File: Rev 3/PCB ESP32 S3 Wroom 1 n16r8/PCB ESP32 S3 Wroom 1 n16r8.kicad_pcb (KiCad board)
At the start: 2 copper layers, 80.5 x 89.5 mm, 37 parts, among them J1 AudioJack3_SwitchT, M1 Haptic Feedback, Q1 BS170, SW1 Home, SW2 Back, SW3 Play/Pause, SW4 Power, SW5 Menu, SW6 Hold, SW7 BOOT_MODE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

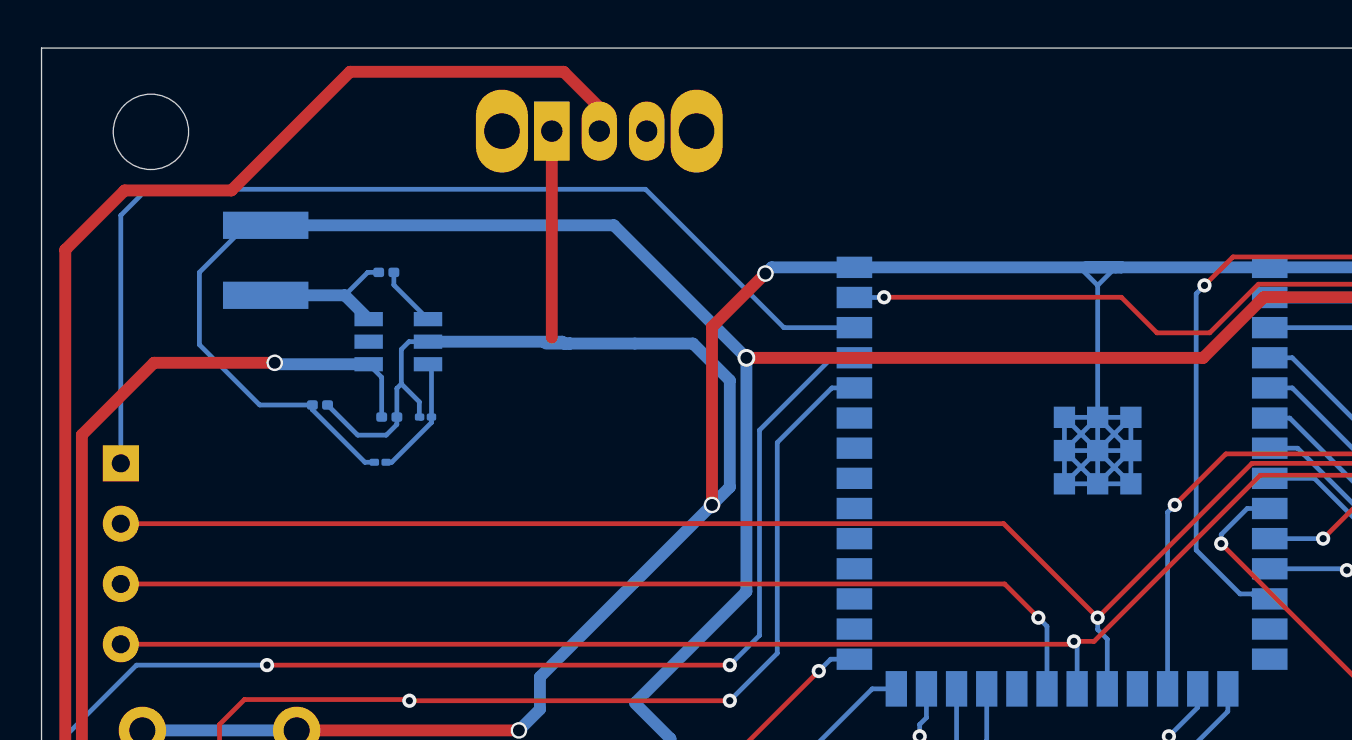
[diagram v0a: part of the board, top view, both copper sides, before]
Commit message: updated power regulator circuit
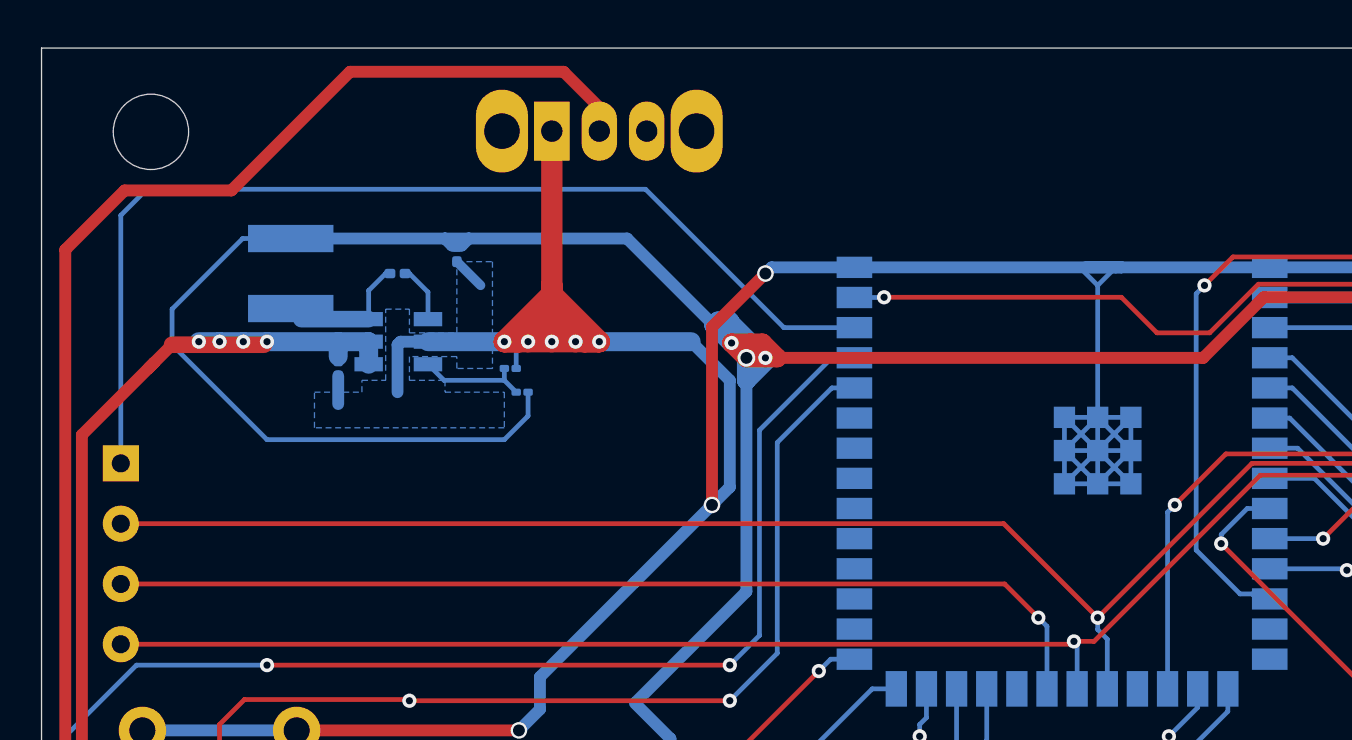
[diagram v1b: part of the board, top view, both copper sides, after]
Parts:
- moved C3 8.59 mm to (76.0, 51.7), turned to 90 degrees
- moved R14 6.67 mm to (78.8, 57.5), turned to 0 degrees
- moved R15 4.12 mm to (78.2, 56.5), turned to 180 degrees
- moved C2 2.97 mm to (71.0, 56.5), turned to 90 degrees
- moved L1 1.19 mm to (69.0, 52.5)
- moved C1 0.48 mm to (73.5, 52.5)
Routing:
- net /VDD: track 359.7 -> 377.0 mm, vias 4 -> 6
- net GND: track 312.9 -> 328.1 mm, vias 3 -> 8
- net /5V: track 99.2 -> 101.8 mm, vias 1 -> 4
- net Net-(U1-SW): track 6.58 -> 5.87 mm
- added copper zone on B.Cu, net GND

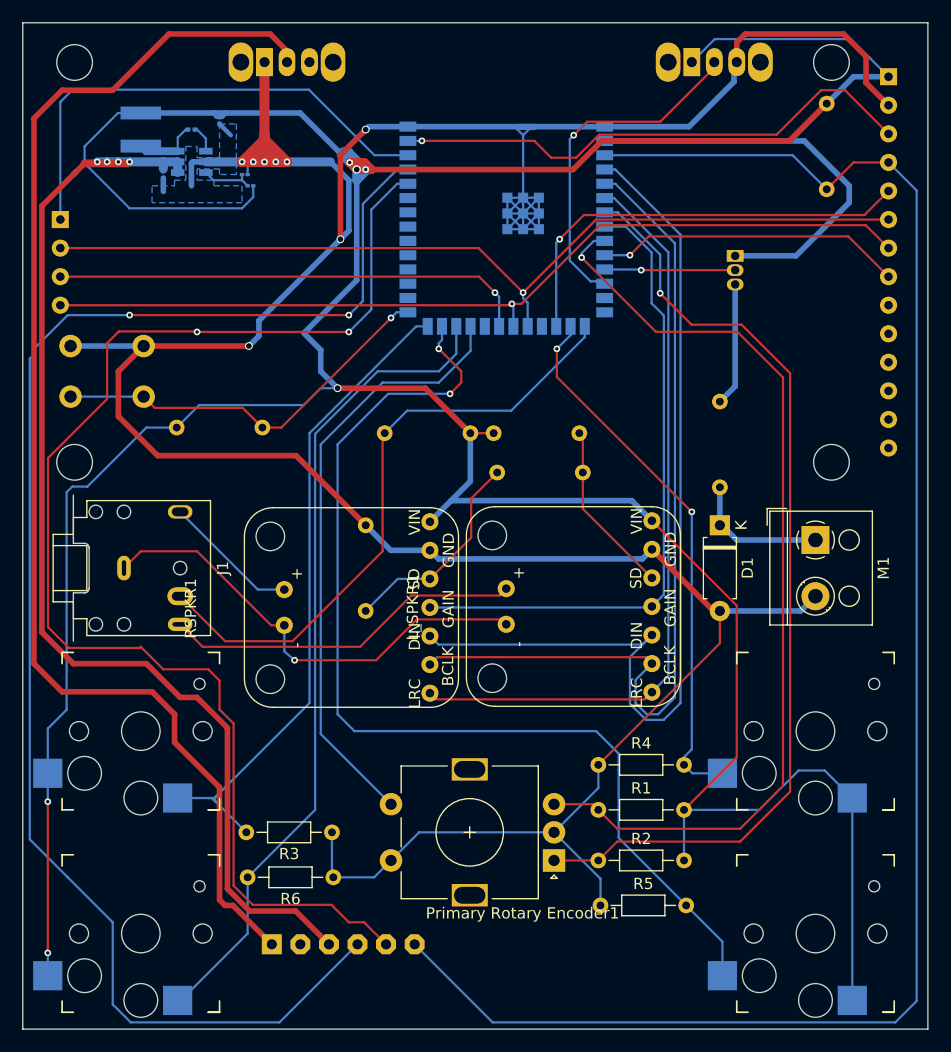
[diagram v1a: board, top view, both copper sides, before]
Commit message: added esp to BOM
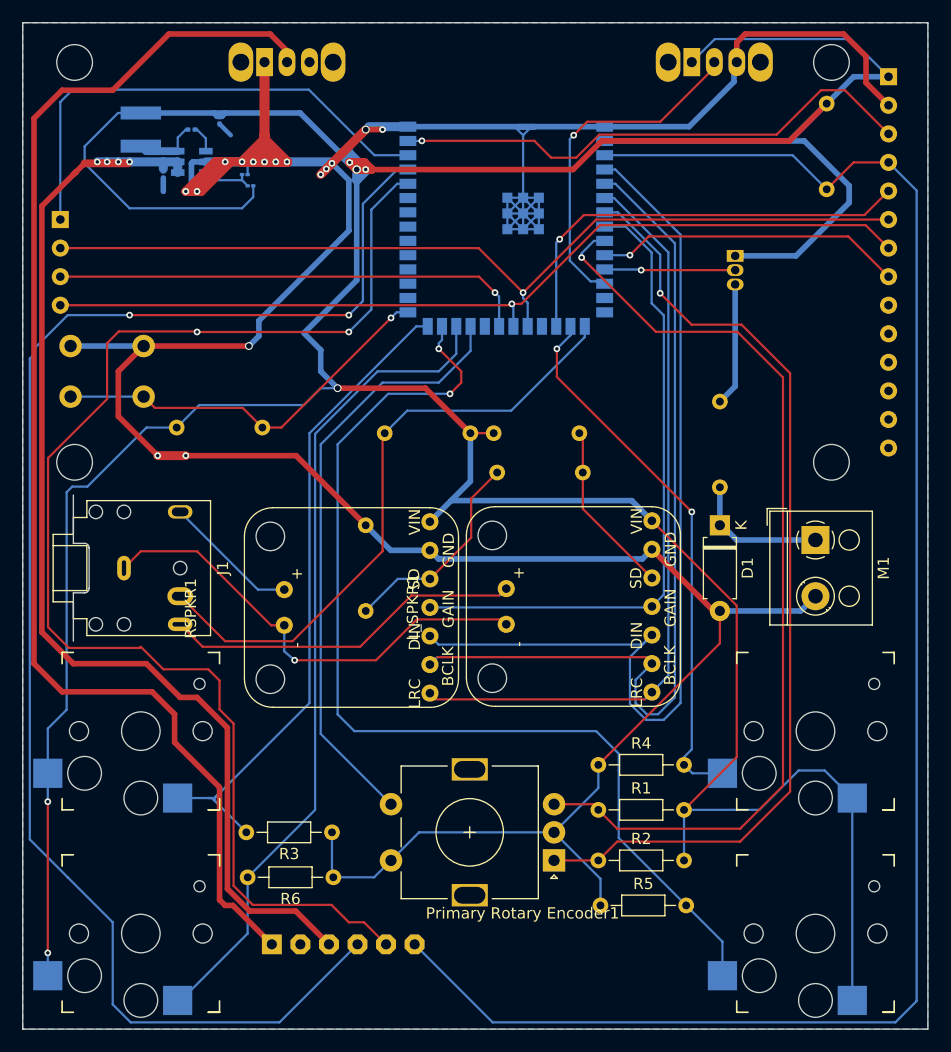
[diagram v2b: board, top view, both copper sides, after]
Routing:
- net GND: track 328.1 -> 340.5 mm, vias 8 -> 16
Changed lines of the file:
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@@
 	)
 	(segment
-		(start 86.75 54.75)
-		(end 89 52.5)
-		(width 0.5)
+		(start 85 56.5)
+		(end 85.5 56)
+		(width 0.8)
 		(layer "F.Cu")
 		(net 7)
@@
 	)
 	(segment
-		(start 67 78)
-		(end 67 74)
-		(width 0.5)
+		(start 73 58)
+		(end 73.5 58)
+		(width 0.8)
 		(layer "F.Cu")
 		(net 7)
@@
 	)
 	(segment
+		(start 67 74)
+		(end 67 78)
+		(width 0.5)
+		(layer "F.Cu")
+		(net 7)
+	)
+	(segment
 		(start 80 54)
 		(end 81.372 55.372)
@@
 	)
 	(segment
+		(start 73 81.5)
+		(end 70.5 81.5)
+		(width 0.8)
+		(layer "F.Cu")
+		(net 7)
+	)
+	(segment
 		(start 119.9315 95.31)
 		(end 120.5 95.31)
@@
 	)
 	(segment
-		(start 86.75 62.25)
-		(end 86.75 54.75)
-		(width 0.5)
-		(layer "F.Cu")
-		(net 7)
-	)
-	(segment
 		(start 80 53.372)
 		(end 82 55.372)
@@
 	)
 	(segment
+		(start 73 58)
+		(end 75.628 55.372)
+		(width 0.8)
+		(layer "F.Cu")
+		(net 7)
+	)
+	(segment
 		(start 89 87.69)
 		(end 82.81 81.5)
@@
 	)
 	(segment
+		(start 69.25 71.75)
+		(end 67 74)
+		(width 0.5)
+		(layer "F.Cu")
+		(net 7)
+	)
+	(segment
+		(start 76.128 55.372)
+		(end 77 55.372)
+		(width 0.8)
+		(layer "F.Cu")
+		(net 7)
+	)
+	(segment
 		(start 81.372 55.372)
 		(end 82 55.372)
@@
 	)
 	(segment
+		(start 85.5 56)
+		(end 86 55.5)
+		(width 0.8)
+		(layer "F.Cu")
+		(net 7)
+	)
+	(segment
 		(start 80 54)
 		(end 78.628 55.372)
@@
 	)
 	(segment
-		(start 67 74)
-		(end 69.25 71.75)
+		(start 133.5 48.34)
+		(end 133.5 46)
 		(width 0.5)
 		(layer "F.Cu")
@@
 	)
 	(segment
-		(start 133.5 48.34)
-		(end 133.5 46)
-		(width 0.5)
+		(start 73.5 58)
+		(end 76.128 55.372)
+		(width 0.8)
 		(layer "F.Cu")
 		(net 7)
@@
 	)
 	(segment
+		(start 67 78)
+		(end 70.5 81.5)
+		(width 0.5)
+		(layer "F.Cu")
+		(net 7)
+	)
+	(segment
+		(start 86 55.5)
+		(end 89 52.5)
+		(width 0.8)
+		(layer "F.Cu")
+		(net 7)
+	)
+	(segment
+		(start 77 55.372)
+		(end 79 55.372)
+		(width 0.8)
+		(layer "F.Cu")
+		(net 7)
+	)
+	(segment
 		(start 80 53)
 		(end 80 54)
@@
 	)
 	(segment
-		(start 70.5 81.5)
-		(end 67 78)
-		(width 0.5)
+		(start 74 58)
+		(end 74.372 58)
+		(width 0.8)
 		(layer "F.Cu")
 		(net 7)
@@
 	)
 	(segment
+		(start 74.372 58)
+		(end 77 55.372)
+		(width 0.8)
+		(layer "F.Cu")
+		(net 7)
+	)
+	(segment
 		(start 80 54.372)
 		(end 79 55.372)
@@
 	)
 	(segment
+		(start 89 52.5)
+		(end 90.5 52.5)
+		(width 0.5)
+		(layer "F.Cu")
+		(net 7)
+	)
+	(segment
 		(start 135.5 50.34)
 		(end 133.5 48.34)
@@
 	)
 	(segment
+		(start 73.5 58)
+		(end 74 58)
+		(width 0.8)
+		(layer "F.Cu")
+		(net 7)
+	)
+	(segment
 		(start 120.5 95.31)
 		(end 120.5 98.19)
@@
 	)
 	(segment
+		(start 75.628 55.372)
+		(end 76.128 55.372)
+		(width 0.8)
+		(layer "F.Cu")
+		(net 7)
+	)
+	(segment
 		(start 82.81 81.5)
-		(end 70.5 81.5)
+		(end 73 81.5)
 		(width 0.5)
 		(layer "F.Cu")
@@
 	)
 	(via
+		(at 86 55.5)
+		(size 0.6)
+		(drill 0.3)
+		(layers "F.Cu" "B.Cu")
+		(net 7)
+	)
+	(via
 		(at 89 52.5)
 		(size 0.7)
@@
 	)
 	(via
+		(at 73 81.5)
+		(size 0.6)
+		(drill 0.3)
+		(layers "F.Cu" "B.Cu")
+		(net 7)
+	)
+	(via
+		(at 76.5 55.372)
+		(size 0.6)
+		(drill 0.3)
+		(layers "F.Cu" "B.Cu")
+		(net 7)
+	)
+	(via
 		(at 78 55.372)
 		(size 0.6)
@@
 	)
 	(via
+		(at 85.5 56)
+		(size 0.6)
+		(drill 0.3)
+		(layers "F.Cu" "B.Cu")
+		(net 7)
+	)
+	(via
 		(at 82 55.372)
 		(size 0.6)
@@
 	)
 	(via
-		(at 86.75 62.25)
+		(at 78.613 71.75)
 		(size 0.7)
 		(drill 0.5)
@@
 	)
 	(via
-		(at 78.613 71.75)
-		(size 0.7)
-		(drill 0.5)
+		(at 85 56.5)
+		(size 0.6)
+		(drill 0.3)
+		(layers "F.Cu" "B.Cu")
+		(net 7)
+	)
+	(via
+		(at 74 58)
+		(size 0.6)
+		(drill 0.3)
+		(layers "F.Cu" "B.Cu")
+		(free yes)
+		(net 7)
+	)
+	(via
+		(at 70.5 81.5)
+		(size 0.6)
+		(drill 0.3)
+		(layers "F.Cu" "B.Cu")
+		(net 7)
+	)
+	(via
+		(at 73 58)
+		(size 0.6)
+		(drill 0.3)
+		(layers "F.Cu" "B.Cu")
+		(free yes)
+		(net 7)
+	)
+	(via
+		(at 90.5 52.5)
+		(size 0.6)
+		(drill 0.3)
 		(layers "F.Cu" "B.Cu")
 		(net 7)
@@
 		(start 92.75 52.24)
 		(end 89.26 52.24)
-		(width 0.5)
+		(width 0.8)
 		(layer "B.Cu")
 		(net 7)
@@
 	)
 	(segment
+		(start 76.5 55.372)
+		(end 74.783 55.372)
+		(width 0.8)
+		(layer "B.Cu")
+		(net 7)
+	)
+	(segment
 		(start 80 46.5)
 		(end 80 47)
@@
 	(segment
 		(start 78.5 55.372)
-		(end 74.783 55.372)
+		(end 76.5 55.372)
 		(width 0.8)
 		(layer "B.Cu")
@@
 	)
 	(zone
+		(net 0)
+		(net_name "")
+		(layer "B.Cu")
+		(name "esp32 blockout")
+		(hatch edge 0.5)
+		(connect_pads
+			(clearance 0)
+		)
+		(min_thickness 0.25)
+		(filled_areas_thickness no)
+		(keepout
+			(tracks allowed)
+			(vias allowed)
+			(pads allowed)
+			(copperpour not_allowed)
+			(footprints allowed)
+		)
+		(fill
+			(thermal_gap 0.5)
+			(thermal_bridge_width 0.5)
+		)
+		(polygon
+			(pts
+				(xy 76 52.5) (xy 126 52.5) (xy 126 43) (xy 76 43)
+			)
+		)
+	)
+	(zone
 		(net 7)
 		(net_name "GND")
 		(layer "B.Cu")
 		(hatch edge 0.5)
+		(priority 1)
 		(connect_pads
 			(clearance 0.5)
@@
 			(thermal_gap 0.5)
 			(thermal_bridge_width 0.5)
-			(island_removal_mode 1)
-			(island_area_min 10)
 		)
 		(polygon
 			(pts
-				(xy 73 54) (xy 74 54) (xy 74 55) (xy 76 55) (xy 76 52) (xy 77.5 52) (xy 77.5 56.5) (xy 76 56.5)
-				(xy 76 56) (xy 74 56) (xy 74 57) (xy 75.5 57) (xy 75.5 57.5) (xy 78 57.5) (xy 78 59) (xy 70 59)
-				(xy 70 57.5) (xy 72 57.5) (xy 72 57) (xy 73 57)
+				(xy 58.5 43) (xy 139 43) (xy 139 132.5) (xy 58.5 132.5)
 			)
 		)

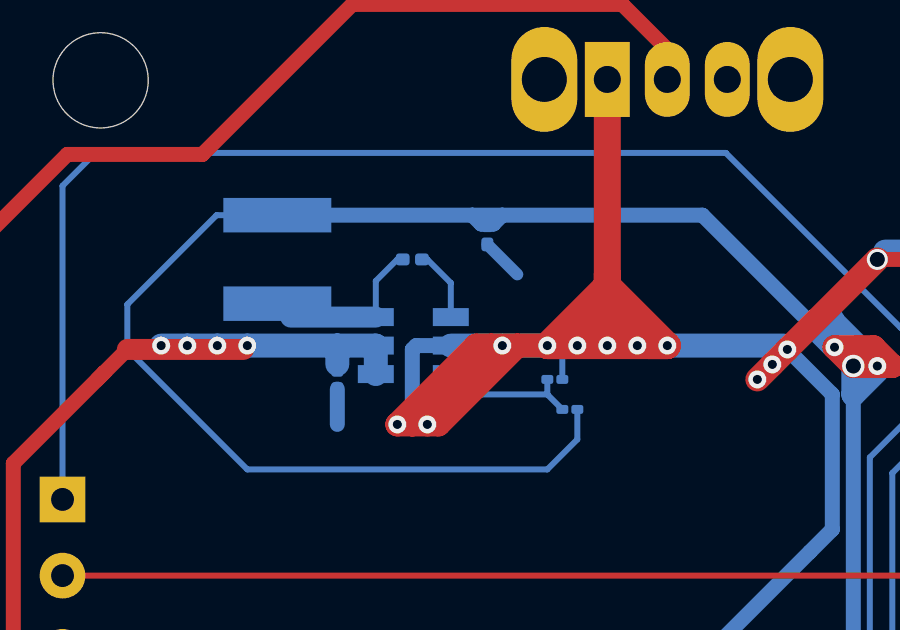
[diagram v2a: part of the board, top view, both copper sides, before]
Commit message: updated pcb and fixed footprints
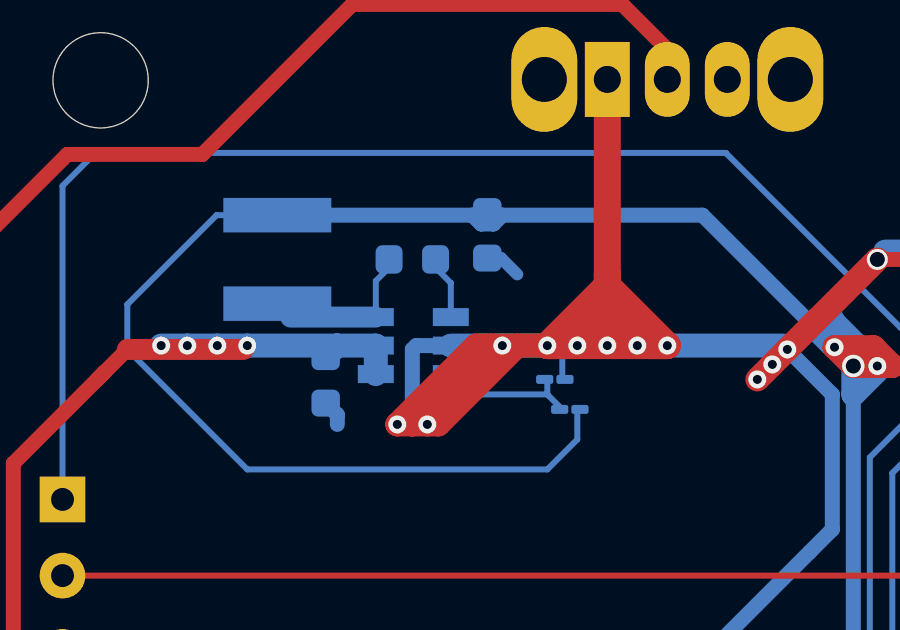
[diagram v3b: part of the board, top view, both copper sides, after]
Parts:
- C1, C2, C3: footprint Capacitor_SMD:C_0201_0603Metric -> Capacitor_SMD:C_0603_1608Metric
- R14, R15: footprint Resistor_SMD:R_01005_0402Metric -> Resistor_SMD:R_01005_0402Metric_Pad0.57x0.30mm_HandSolder
- moved C2 0.39 mm to (70.6, 56.5)
